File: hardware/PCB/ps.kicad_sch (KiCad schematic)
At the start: 14 parts, among them U10 TPS2121RUXR, U9 TPS54308

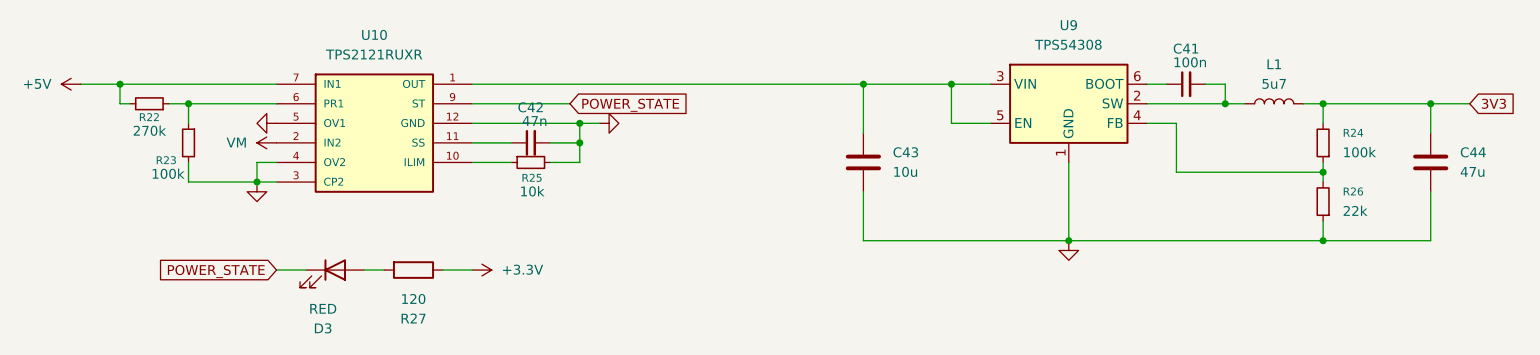
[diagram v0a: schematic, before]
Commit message: Finished schematic for LoRa, added BME280
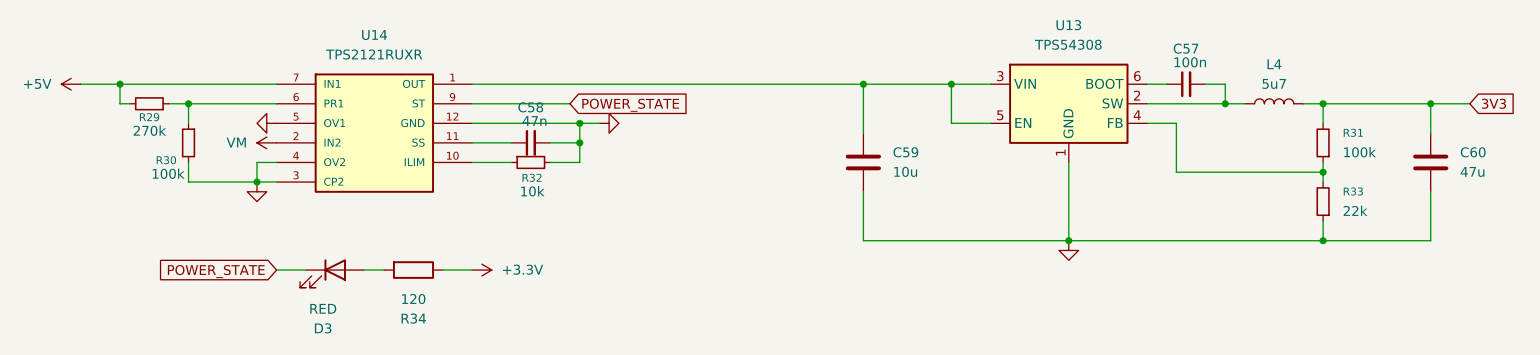
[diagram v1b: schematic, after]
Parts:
- renumbered C41 to C57, C42 to C58, C43 to C59, C44 to C60, L1 to L4, R22 to R29, R23 to R30, R24 to R31, R25 to R32, R26 to R33, R27 to R34, U9 to U13, U10 to U14
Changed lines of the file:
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@@
 		(on_board yes)
 		(dnp no)
-		(property "Reference" "C42"
+		(property "Reference" "C58"
 			(at 88.9 57.658 90)
 			(effects
@@
 			(project "Startracker"
 				(path "/45ea479c-a8ef-4c14-88b0-391ede4fd156/afb5d1bc-fe1e-400f-ae7a-b48aaf074925"
-					(reference "C42")
+					(reference "C58")
 					(unit 1)
 				)
@@
 		(dnp no)
 		(fields_autoplaced yes)
-		(property "Reference" "U10"
+		(property "Reference" "U14"
 			(at 68.58 48.26 0)
 			(effects
@@
 			(project "Startracker"
 				(path "/45ea479c-a8ef-4c14-88b0-391ede4fd156/afb5d1bc-fe1e-400f-ae7a-b48aaf074925"
-					(reference "U10")
+					(reference "U14")
 					(unit 1)
 				)
@@
 		(dnp no)
 		(fields_autoplaced yes)
-		(property "Reference" "C44"
+		(property "Reference" "C60"
 			(at 209.55 63.4999 0)
 			(effects
@@
 			(project "Startracker"
 				(path "/45ea479c-a8ef-4c14-88b0-391ede4fd156/afb5d1bc-fe1e-400f-ae7a-b48aaf074925"
-					(reference "C44")
+					(reference "C60")
 					(unit 1)
 				)
@@
 		(dnp no)
 		(fields_autoplaced yes)
-		(property "Reference" "C43"
+		(property "Reference" "C59"
 			(at 135.89 63.4999 0)
 			(effects
@@
 			(project ""
 				(path "/45ea479c-a8ef-4c14-88b0-391ede4fd156/afb5d1bc-fe1e-400f-ae7a-b48aaf074925"
-					(reference "C43")
+					(reference "C59")
 					(unit 1)
 				)
@@
 		(dnp no)
 		(fields_autoplaced yes)
-		(property "Reference" "#PWR085"
+		(property "Reference" "#PWR0119"
 			(at 77.47 78.74 0)
 			(effects
@@
 			(project "Startracker"
 				(path "/45ea479c-a8ef-4c14-88b0-391ede4fd156/afb5d1bc-fe1e-400f-ae7a-b48aaf074925"
-					(reference "#PWR085")
+					(reference "#PWR0119")
 					(unit 1)
 				)
@@
 		(dnp no)
 		(fields_autoplaced yes)
-		(property "Reference" "R24"
+		(property "Reference" "R31"
 			(at 194.31 60.9599 0)
 			(effects
@@
 			(project ""
 				(path "/45ea479c-a8ef-4c14-88b0-391ede4fd156/afb5d1bc-fe1e-400f-ae7a-b48aaf074925"
-					(reference "R24")
+					(reference "R31")
 					(unit 1)
 				)
@@
 		(dnp no)
 		(fields_autoplaced yes)
-		(property "Reference" "R26"
+		(property "Reference" "R33"
 			(at 194.31 68.5799 0)
 			(effects
@@
 			(project "Startracker"
 				(path "/45ea479c-a8ef-4c14-88b0-391ede4fd156/afb5d1bc-fe1e-400f-ae7a-b48aaf074925"
-					(reference "R26")
+					(reference "R33")
 					(unit 1)
 				)
@@
 		(on_board yes)
 		(dnp no)
-		(property "Reference" "R22"
+		(property "Reference" "R29"
 			(at 39.37 58.928 90)
 			(effects
@@
 			(project "Startracker"
 				(path "/45ea479c-a8ef-4c14-88b0-391ede4fd156/afb5d1bc-fe1e-400f-ae7a-b48aaf074925"
-					(reference "R22")
+					(reference "R29")
 					(unit 1)
 				)
@@
 		(dnp no)
 		(fields_autoplaced yes)
-		(property "Reference" "#PWR084"
+		(property "Reference" "#PWR0118"
 			(at 158.75 81.28 0)
 			(effects
@@
 			(project "Startracker"
 				(path "/45ea479c-a8ef-4c14-88b0-391ede4fd156/afb5d1bc-fe1e-400f-ae7a-b48aaf074925"
-					(reference "#PWR084")
+					(reference "#PWR0118")
 					(unit 1)
 				)
@@
 		(dnp no)
 		(fields_autoplaced yes)
-		(property "Reference" "U9"
+		(property "Reference" "U13"
 			(at 158.75 46.99 0)
 			(effects
@@
 			(project ""
 				(path "/45ea479c-a8ef-4c14-88b0-391ede4fd156/afb5d1bc-fe1e-400f-ae7a-b48aaf074925"
-					(reference "U9")
+					(reference "U13")
 					(unit 1)
 				)
@@
 		(dnp no)
 		(fields_autoplaced yes)
-		(property "Reference" "#PWR078"
+		(property "Reference" "#PWR0113"
 			(at 34.29 54.61 0)
 			(effects
@@
 			(project "Startracker"
 				(path "/45ea479c-a8ef-4c14-88b0-391ede4fd156/afb5d1bc-fe1e-400f-ae7a-b48aaf074925"
-					(reference "#PWR078")
+					(reference "#PWR0113")
 					(unit 1)
 				)
@@
 		(on_board yes)
 		(dnp no)
-		(property "Reference" "C41"
+		(property "Reference" "C57"
 			(at 173.99 50.038 90)
 			(effects
@@
 			(project "Startracker"
 				(path "/45ea479c-a8ef-4c14-88b0-391ede4fd156/afb5d1bc-fe1e-400f-ae7a-b48aaf074925"
-					(reference "C41")
+					(reference "C57")
 					(unit 1)
 				)
@@
 		(dnp no)
 		(fields_autoplaced yes)
-		(property "Reference" "#PWR080"
+		(property "Reference" "#PWR0114"
 			(at 49.53 59.69 0)
 			(effects
@@
 			(project "Startracker"
 				(path "/45ea479c-a8ef-4c14-88b0-391ede4fd156/afb5d1bc-fe1e-400f-ae7a-b48aaf074925"
-					(reference "#PWR080")
+					(reference "#PWR0114")
 					(unit 1)
 				)
@@
 		(on_board yes)
 		(dnp no)
-		(property "Reference" "R25"
+		(property "Reference" "R32"
 			(at 90.424 66.802 90)
 			(effects
@@
 			(project "Startracker"
 				(path "/45ea479c-a8ef-4c14-88b0-391ede4fd156/afb5d1bc-fe1e-400f-ae7a-b48aaf074925"
-					(reference "R25")
+					(reference "R32")
 					(unit 1)
 				)
@@
 		(dnp no)
 		(fields_autoplaced yes)
-		(property "Reference" "#PWR081"
+		(property "Reference" "#PWR0115"
 			(at 104.14 59.69 0)
 			(effects
@@
 			(project "Startracker"
 				(path "/45ea479c-a8ef-4c14-88b0-391ede4fd156/afb5d1bc-fe1e-400f-ae7a-b48aaf074925"
-					(reference "#PWR081")
+					(reference "#PWR0115")
 					(unit 1)
 				)
@@
 		(dnp no)
 		(fields_autoplaced yes)
-		(property "Reference" "R27"
+		(property "Reference" "R34"
 			(at 73.66 85.09 90)
 			(effects
@@
 			(project "Startracker"
 				(path "/45ea479c-a8ef-4c14-88b0-391ede4fd156/afb5d1bc-fe1e-400f-ae7a-b48aaf074925"
-					(reference "R27")
+					(reference "R34")
 					(unit 1)
 				)
@@
 		(dnp no)
 		(fields_autoplaced yes)
-		(property "Reference" "L1"
+		(property "Reference" "L4"
 			(at 185.42 52.07 90)
 			(effects
@@
 			(project ""
 				(path "/45ea479c-a8ef-4c14-88b0-391ede4fd156/afb5d1bc-fe1e-400f-ae7a-b48aaf074925"
-					(reference "L1")
+					(reference "L4")
 					(unit 1)
 				)
@@
 		(dnp no)
 		(fields_autoplaced yes)
-		(property "Reference" "#PWR083"
+		(property "Reference" "#PWR0117"
 			(at 53.34 73.66 0)
 			(effects
@@
 			(project "Startracker"
 				(path "/45ea479c-a8ef-4c14-88b0-391ede4fd156/afb5d1bc-fe1e-400f-ae7a-b48aaf074925"
-					(reference "#PWR083")
+					(reference "#PWR0117")
 					(unit 1)
 				)
@@
 		(dnp no)
 		(fields_autoplaced yes)
-		(property "Reference" "#PWR082"
+		(property "Reference" "#PWR0116"
 			(at 59.69 62.23 0)
 			(effects
@@
 			(project ""
 				(path "/45ea479c-a8ef-4c14-88b0-391ede4fd156/afb5d1bc-fe1e-400f-ae7a-b48aaf074925"
-					(reference "#PWR082")
+					(reference "#PWR0116")
 					(unit 1)
 				)
@@
 		(on_board yes)
 		(dnp no)
-		(property "Reference" "R23"
+		(property "Reference" "R30"
 			(at 42.926 64.516 0)
 			(effects
@@
 			(project "Startracker"
 				(path "/45ea479c-a8ef-4c14-88b0-391ede4fd156/afb5d1bc-fe1e-400f-ae7a-b48aaf074925"
-					(reference "R23")
-					(unit 1)
-				)
+					(reference "R30")
+					(unit 1)
+				)

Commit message: Finished parts sourcing and added missing footprints
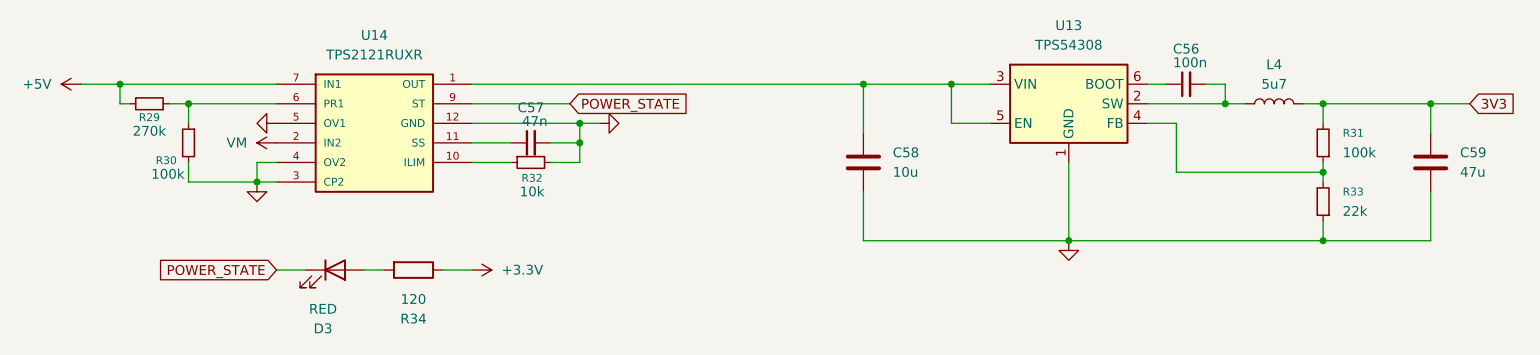
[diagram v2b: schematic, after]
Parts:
- renumbered C57 to C56, C58 to C57, C59 to C58, C60 to C59
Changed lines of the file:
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@@
 		(on_board yes)
 		(dnp no)
-		(property "Reference" "C58"
+		(property "Reference" "C57"
 			(at 88.9 57.658 90)
 			(effects
@@
 			(project "Startracker"
 				(path "/45ea479c-a8ef-4c14-88b0-391ede4fd156/afb5d1bc-fe1e-400f-ae7a-b48aaf074925"
-					(reference "C58")
+					(reference "C57")
 					(unit 1)
 				)
@@
 		(dnp no)
 		(fields_autoplaced yes)
-		(property "Reference" "C60"
+		(property "Reference" "C59"
 			(at 209.55 63.4999 0)
 			(effects
@@
 			(project "Startracker"
 				(path "/45ea479c-a8ef-4c14-88b0-391ede4fd156/afb5d1bc-fe1e-400f-ae7a-b48aaf074925"
-					(reference "C60")
+					(reference "C59")
 					(unit 1)
 				)
@@
 		(dnp no)
 		(fields_autoplaced yes)
-		(property "Reference" "C59"
+		(property "Reference" "C58"
 			(at 135.89 63.4999 0)
 			(effects
@@
 			(project ""
 				(path "/45ea479c-a8ef-4c14-88b0-391ede4fd156/afb5d1bc-fe1e-400f-ae7a-b48aaf074925"
-					(reference "C59")
+					(reference "C58")
 					(unit 1)
 				)
@@
 		(on_board yes)
 		(dnp no)
-		(property "Reference" "C57"
+		(property "Reference" "C56"
 			(at 173.99 50.038 90)
 			(effects
@@
 			(project "Startracker"
 				(path "/45ea479c-a8ef-4c14-88b0-391ede4fd156/afb5d1bc-fe1e-400f-ae7a-b48aaf074925"
-					(reference "C57")
-					(unit 1)
-				)
+					(reference "C56")
+					(unit 1)
+				)
